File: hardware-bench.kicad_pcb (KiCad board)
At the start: 2 copper layers, 3 parts, among them U2 CR2013-MI2120

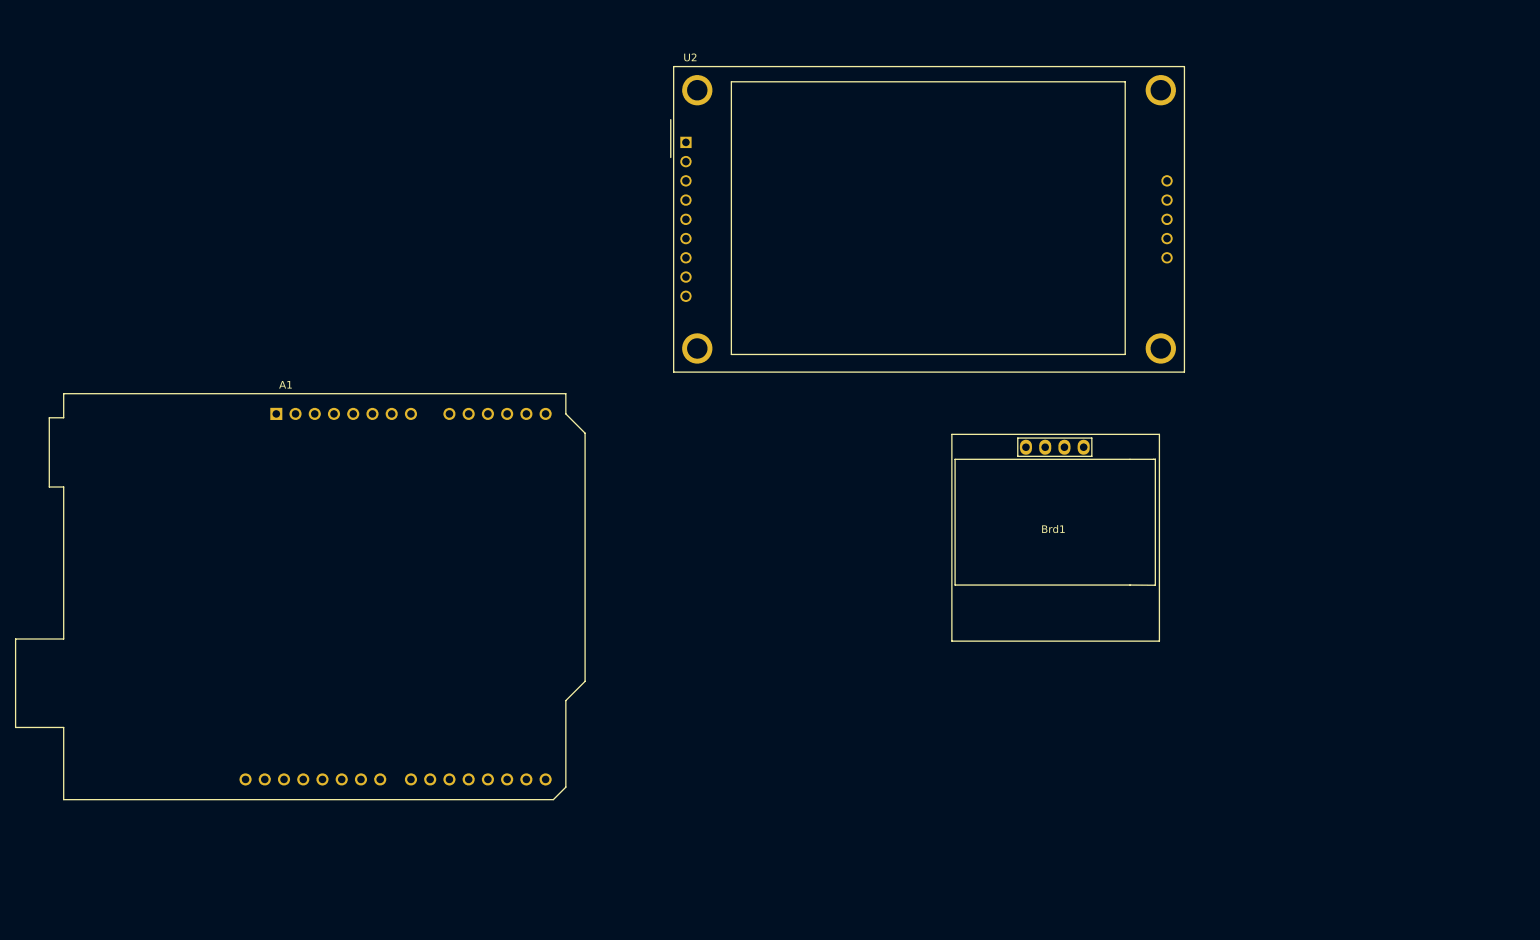
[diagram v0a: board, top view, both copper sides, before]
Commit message: Raspberry PI Pico hardware bench (#2)
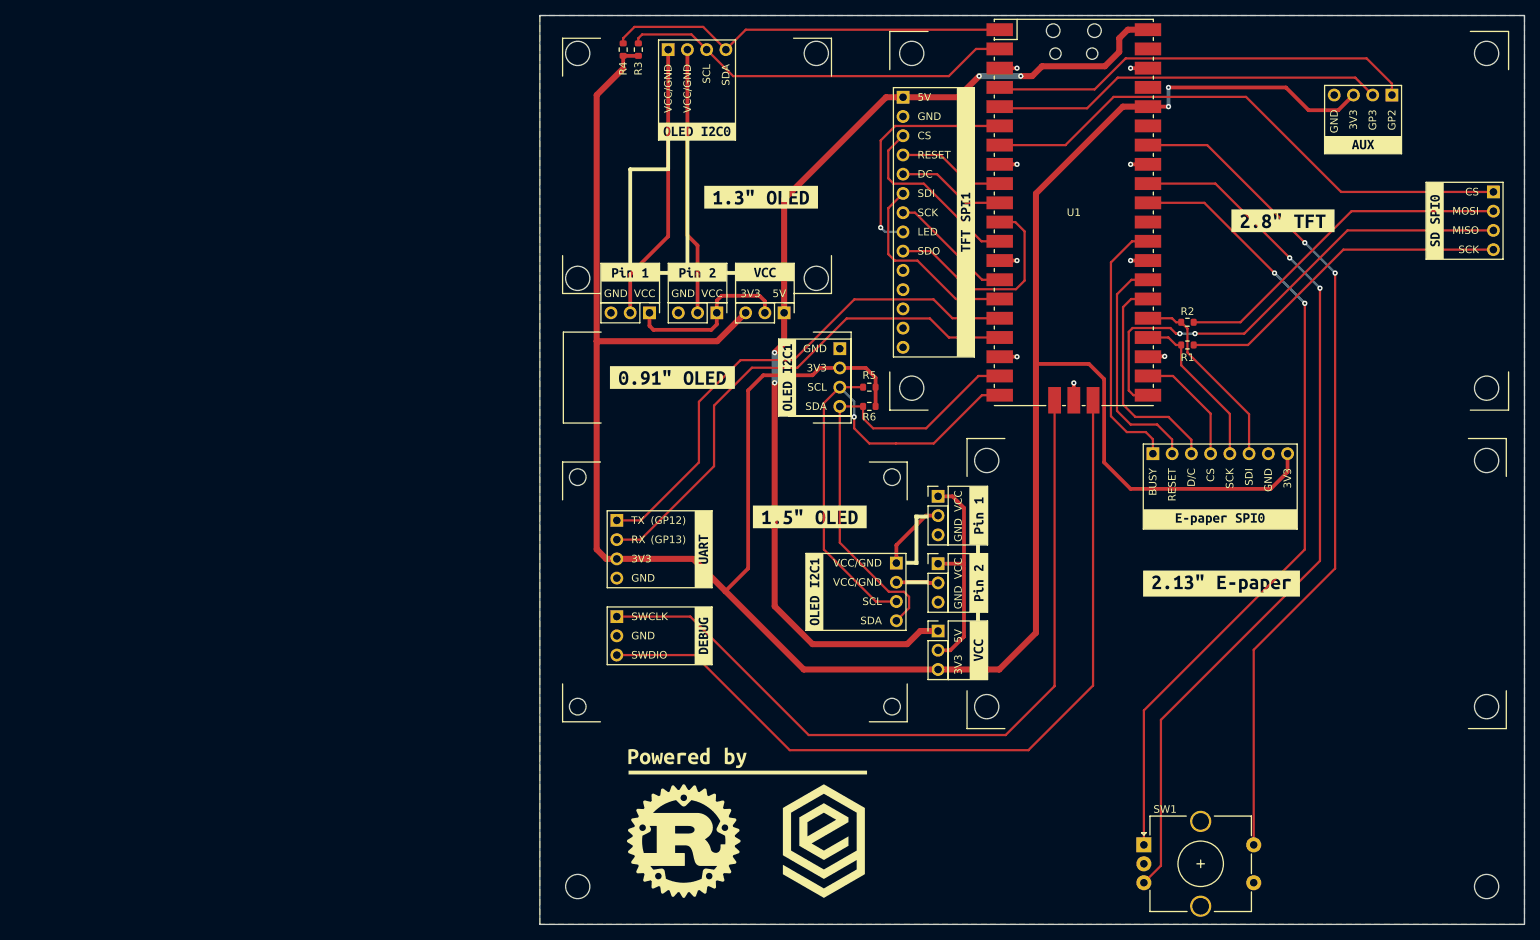
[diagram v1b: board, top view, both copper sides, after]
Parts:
- removed A1: Arduino_UNO_R2, Module:Arduino_UNO_R2
- removed Brd1: SSD1306, SSD1306:128x64OLED
- removed U2: CR2013-MI2120, Display:CR2013-MI2120
- added DS1: EPaper-2.3, hardware-bench:EPaper-2.13, F.Cu at (192.0, 105.0)
- added DS2: TFT_2.8_240x320, hardware-bench:TFT_2.8_240x320, F.Cu at (187.1, 57.1)
- added DS3: GME12864-80, hardware-bench:GME12864-80, F.Cu at (120.8, 49.9)
- added DS4: GME128128-02, hardware-bench:GME128128-02, F.Cu at (125.8, 106.1)
- added DS5: OLED_0.91, hardware-bench:OLED_0.91, F.Cu at (122.1, 77.8)
- added H1: MountingHole, MountingHole:MountingHole_3.2mm_M3, F.Cu at (105.0, 145.0)
- added H2: MountingHole, MountingHole:MountingHole_3.2mm_M3, F.Cu at (225.0, 145.0)
- added J1: Conn_01x04_Male, hardware-bench:PinHeader_1x04_P2.54mm_Horizontal_Flipped, F.Cu at (110.2, 96.7)
- added J2: Conn_01x03_Male, hardware-bench:PinHeader_1x03_P2.54mm_Horizontal_Flipped, F.Cu at (110.2, 109.4)
- added J3: Conn_01x04_Male, hardware-bench:PinHeader_1x04_P2.54mm_Horizontal_Flipped, F.Cu at (212.5, 40.5)
- added JP1: Jumper_3_Open, Connector_PinHeader_2.54mm:PinHeader_1x03_P2.54mm_Vertical, F.Cu at (132.2, 69.2)
- added JP2: Jumper_3_Open, Connector_PinHeader_2.54mm:PinHeader_1x03_P2.54mm_Vertical, F.Cu at (114.5, 69.2)
- added JP3: Jumper_3_Open, Connector_PinHeader_2.54mm:PinHeader_1x03_P2.54mm_Vertical, F.Cu at (123.4, 69.2)
- added JP4: Jumper_3_Open, Connector_PinHeader_2.54mm:PinHeader_1x03_P2.54mm_Vertical, F.Cu at (152.6, 111.3)
- added JP5: Jumper_3_Open, Connector_PinHeader_2.54mm:PinHeader_1x03_P2.54mm_Vertical, F.Cu at (152.6, 102.4)
- added JP6: Jumper_3_Open, Connector_PinHeader_2.54mm:PinHeader_1x03_P2.54mm_Vertical, F.Cu at (152.6, 93.5)
- added LOGO1: Logo_Rust, hardware-bench:Logo_Rust, F.Cu at (119.0, 139.0)
- added LOGO2: Logo_E_G, hardware-bench:Logo_E_G, F.Cu at (137.5, 139.0)
- added R1: 0, Resistor_SMD:R_0603_1608Metric, F.Cu at (185.5, 73.5)
- added R2: 0, Resistor_SMD:R_0603_1608Metric, F.Cu at (185.5, 70.5)
- added R3: DNP, Resistor_SMD:R_0603_1608Metric, F.Cu at (113.0, 34.5)
- added R4: DNP, Resistor_SMD:R_0603_1608Metric, F.Cu at (111.0, 34.5)
- added R5: DNP, Resistor_SMD:R_0603_1608Metric, F.Cu at (143.5, 79.1)
- added R6: DNP, Resistor_SMD:R_0603_1608Metric, F.Cu at (143.5, 81.6)
- added SW1: RotaryEncoder_Switch, Rotary_Encoder:RotaryEncoder_Alps_EC12E-Switch_Vertical_H20mm_CircularMountingHoles, F.Cu at (179.8, 139.5)
- added U1: Pico, hardware-bench:RPi_Pico_SMD, F.Cu at (170.5, 56.0)
- added kibuzzard-635BBA92: G***, kibuzzard-635BBA92, F.Cu at (119.5, 128.0)
- added kibuzzard-636E891A: G***, kibuzzard-636E891A, F.Cu at (132.7, 77.8)
- added kibuzzard-636E891A: G***, kibuzzard-636E891A, F.Cu at (136.3, 106.1)
- added kibuzzard-636E891A: G***, kibuzzard-636E891A, B.Cu at (136.3, 106.1)
- added kibuzzard-636E891A: G***, kibuzzard-636E891A, B.Cu at (132.7, 77.8)
- added kibuzzard-636E8B55: G***, kibuzzard-636E8B55, F.Cu at (121.6, 100.5)
- added kibuzzard-636E8B55: G***, kibuzzard-636E8B55, B.Cu at (121.6, 100.5)
- added kibuzzard-636E8BC3: G***, kibuzzard-636E8BC3, F.Cu at (121.6, 111.9)
- added kibuzzard-636E8BC3: G***, kibuzzard-636E8BC3, B.Cu at (121.6, 111.9)
- added kibuzzard-636E8C97: G***, kibuzzard-636E8C97, F.Cu at (120.8, 45.3)
- added kibuzzard-636E8C97: G***, kibuzzard-636E8C97, B.Cu at (120.8, 45.3)
- added kibuzzard-636E8D2A: G***, kibuzzard-636E8D2A, F.Cu at (218.2, 57.1)
- added kibuzzard-636E8D2A: G***, kibuzzard-636E8D2A, B.Cu at (218.3, 57.1)
- added kibuzzard-636E8D77: G***, kibuzzard-636E8D77, F.Cu at (208.7, 47.0)
- added kibuzzard-636E8D77: G***, kibuzzard-636E8D77, B.Cu at (208.7, 47.0)
- added kibuzzard-636E8E76: G***, kibuzzard-636E8E76, F.Cu at (189.8, 96.5)
- added kibuzzard-636E8E76: G***, kibuzzard-636E8E76, B.Cu at (189.8, 96.5)
- added kibuzzard-636E8FDA: G***, kibuzzard-636E8FDA, F.Cu at (156.2, 57.3)
- added kibuzzard-636E8FDA: G***, kibuzzard-636E8FDA, B.Cu at (156.2, 57.3)
- added kibuzzard-636E96FA: G***, kibuzzard-636E96FA, F.Cu at (157.9, 96.0)
- added kibuzzard-636E9700: G***, kibuzzard-636E9700, F.Cu at (157.9, 104.9)
- added kibuzzard-636E9707: G***, kibuzzard-636E9707, F.Cu at (157.9, 113.8)
- added kibuzzard-636E9711: G***, kibuzzard-636E9711, F.Cu at (129.7, 63.9)
- added kibuzzard-636E971C: G***, kibuzzard-636E971C, F.Cu at (111.9, 63.9)
- added kibuzzard-636E9726: G***, kibuzzard-636E9726, F.Cu at (120.8, 63.9)
- added kibuzzard-636EACB9: G***, kibuzzard-636EACB9, B.Cu at (206.5, 101.0)
- added kibuzzard-636EB715: G***, kibuzzard-636EB715, F.Cu at (129.2, 54.0)
- added kibuzzard-636EB722: G***, kibuzzard-636EB722, F.Cu at (117.5, 77.8)
- added kibuzzard-636EB72B: G***, kibuzzard-636EB72B, F.Cu at (135.6, 96.2)
- added kibuzzard-636EB734: G***, kibuzzard-636EB734, F.Cu at (190.0, 105.0)
- added kibuzzard-636EB73F: G***, kibuzzard-636EB73F, F.Cu at (198.1, 57.1)
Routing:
- net +3V3: track 0.00 -> 365.6 mm, vias 0 -> 2
- net +5V: track 0.00 -> 136.1 mm, vias 0 -> 4
- net /ENCODER_B: track 0.00 -> 117.5 mm, vias 0 -> 2
- net /ENCODER_SW: track 0.00 -> 112.6 mm, vias 0 -> 2
- net /DEBUG_SWDIO: track 0.00 -> 110.2 mm
- net /ENCODER_A: track 0.00 -> 107.4 mm, vias 0 -> 2
- net /DEBUG_SWCLK: track 0.00 -> 105.6 mm
- net /SD_~{CS}: track 0.00 -> 72.1 mm
- net /UART_RX: track 0.00 -> 69.3 mm
- net /UART_TX: track 0.00 -> 69.3 mm
- net /I2C1_SCL: track 0.00 -> 67.6 mm, vias 0 -> 1
- net /SD_MISO: track 0.00 -> 63.9 mm, vias 0 -> 2
- net /I2C1_SDA: track 0.00 -> 60.9 mm
- net /AUX_GP2: track 0.00 -> 55.6 mm
- net /I2C0_SDA: track 0.00 -> 54.2 mm
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- added copper zone on B.Cu, net GND
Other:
- board outline added: 130 x 120 mm
- board text added: "(GP12)"
- board text added: "(GP13)"
- board text added: "0.91{dblquote} OLED Resolution: 128x32 Controller: SSD1306 1.3{dblquote} OLED Model: GME12864-80 Resolution: 128x64 Controller: SH1106 1.5{dblquote} OLED Model: GME128128-02 Resolution: 128x128 Controller: SSD1327 2.8{dblquote} TFT Resolution: 320x240 Controller: ILI9341 2.13{dblquote} E-paper Model: MH-ET LIVE 2.13 Inch E-paper Module Resolution: 250x122 EPD Module: GDEY0213Z98 Controller: SSD16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"
- board text added: "3V3"
- board text added: "5V"
- board text added: "BUSY"
- board text added: "CS"
- board text added: "D/C"
- board text added: "DC"
- board text added: "GND"
- board text added: "GP2"
- board text added: "GP3"
- board text added: "LED"
- board text added: "MISO"
- board text added: "MOSI"
- board text added: "RESET"
- board text added: "RX"
- board text added: "SCK"
- board text added: "SCL"
- board text added: "SDA"
- board text added: "SDI"
- board text added: "SDO"
- board text added: "SWCLK"
- board text added: "SWDIO"
- board text added: "TX"
- board text added: "VCC"
- board text added: "VCC/GND"
